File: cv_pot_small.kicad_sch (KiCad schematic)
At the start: 13 parts, among them J1 I/O connector, U1 HT7550-1, U2 TLV6001UIDBVR

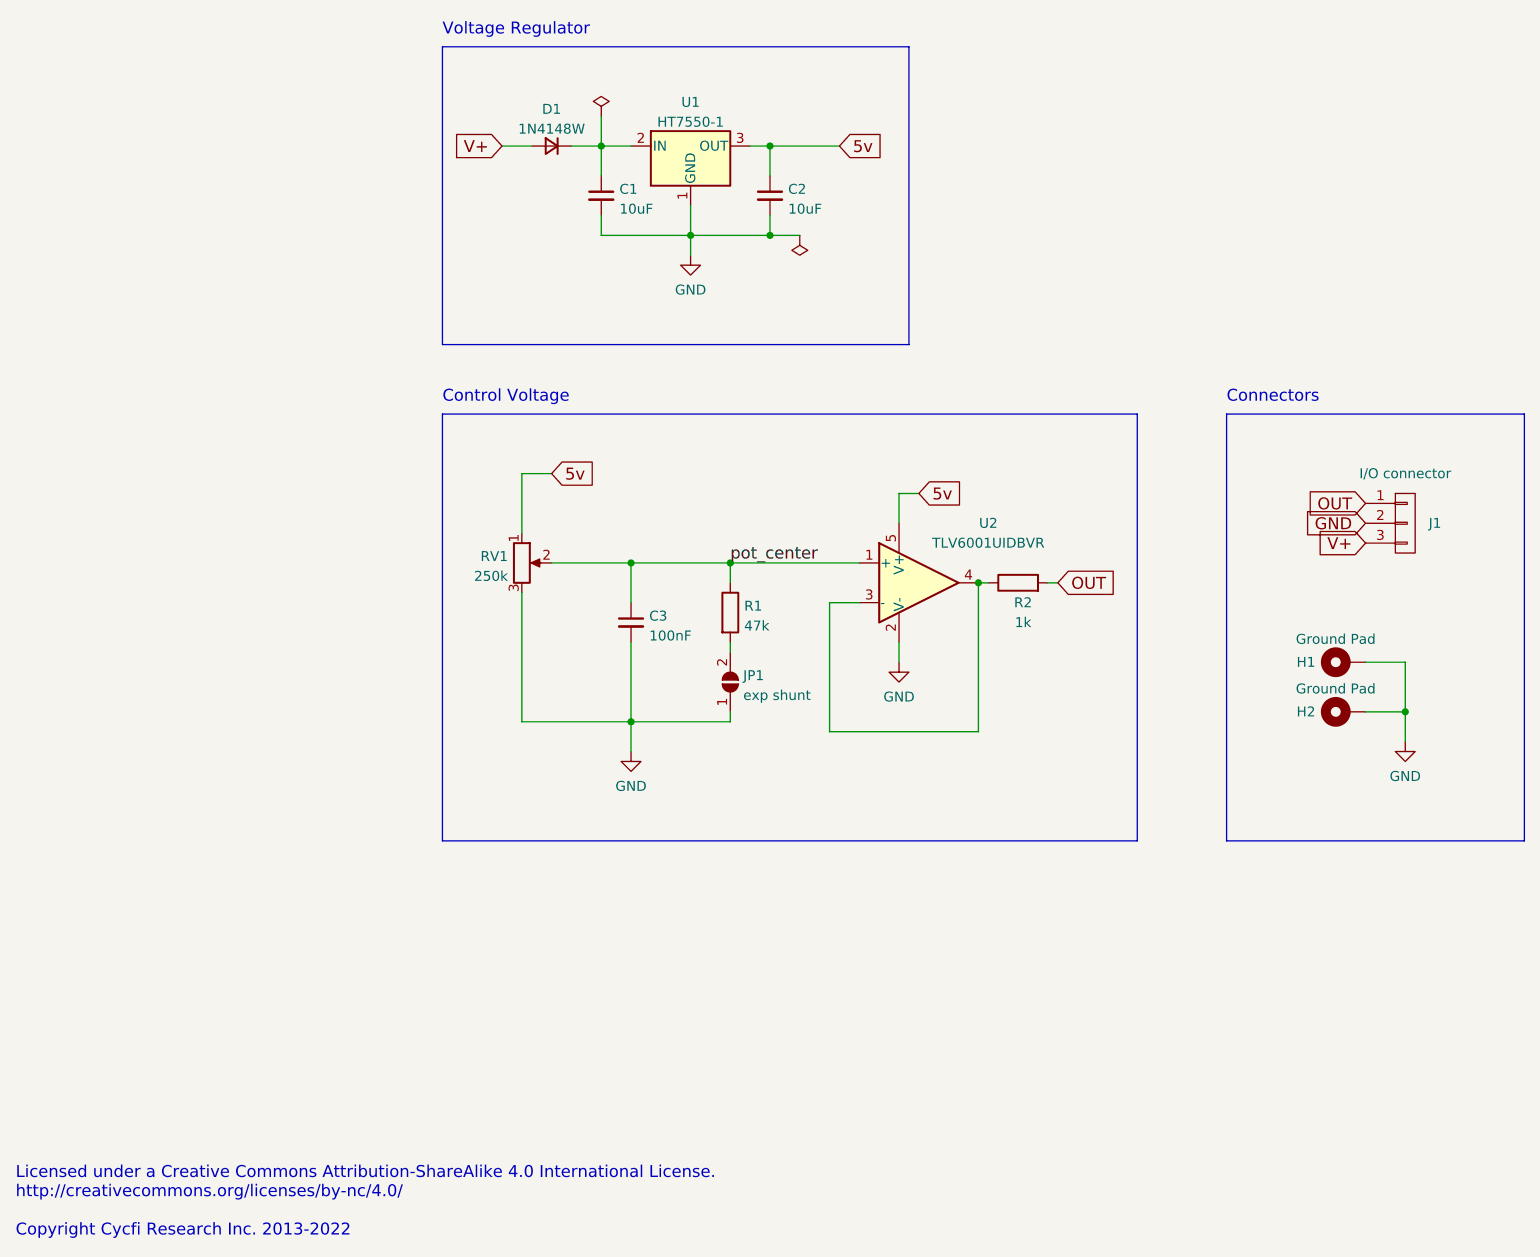
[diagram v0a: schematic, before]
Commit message: Convert the small CV pot to the 3.3V CV port standard
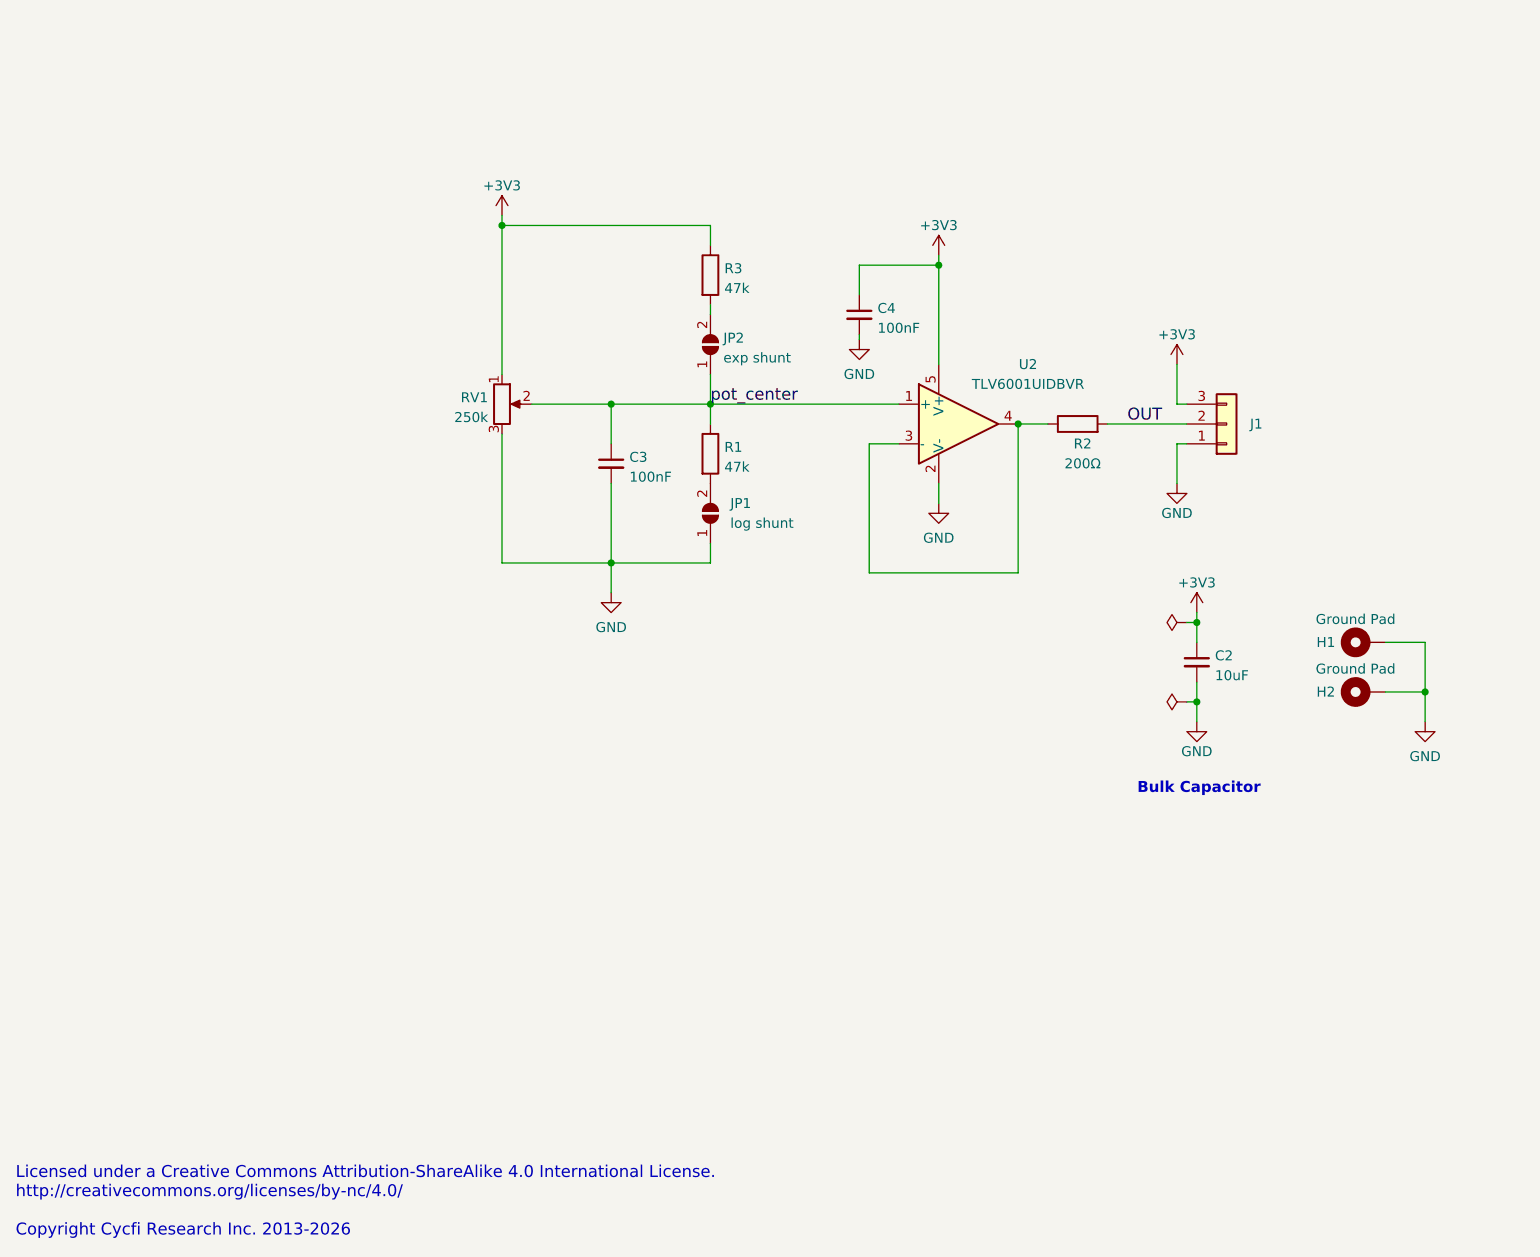
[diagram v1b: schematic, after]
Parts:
- removed C1: 10uF, Capacitor_SMD:C_0805_2012Metric, symbol Device:C_Small
- removed D1: 1N4148W, Diode_SMD:D_SOD-123, symbol Device:D_Small
- removed U1: HT7550-1, Package_TO_SOT_SMD:SOT-89-3, symbol cycfi_library:sot89-3-gio
- added C4: 100nF, Capacitor_SMD:C_0402_1005Metric, symbol Device:C_Small
- added JP2: exp shunt, Jumper:SolderJumper-2_P1.3mm_Open_TrianglePad1.0x1.5mm, symbol Jumper:SolderJumper_2_Open
- added R3: 47k, Resistor_SMD:R_0402_1005Metric, symbol Device:R
- J1: footprint cycfi_library:pin_header_1x3p_2.54mm_smd_horizontal -> Connector_JST:JST_SH_SM03B-SRSS-TB_1x03-1MP_P1.00mm_Horizontal; symbol cycfi_library:conn_1x3 -> Connector_Generic:Conn_01x03; LCSC (none) -> C160403
- JP1: value exp shunt -> log shunt
- R2: value 1k -> 200Ω; LCSC C11702 -> C25087
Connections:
- net V+ is gone; now on net +3V3: J1.3 (Pin_3)
- net GND: now also J1.1 (Pin_1), C4.2; no longer J1.2 (P2)
- net OUT: now also J1.2 (Pin_2); no longer J1.1 (P1)
- net pot_center: now also JP2.1 (A)
- net 5v renamed +3V3
- net +3V3: now also C4.1, R3.1
- new net: JP2.2 (B), R3.2
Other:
- note added: "Bulk Capacitor"
- note added: "Licensed under a Creative Commons Attribution-ShareAlike 4.0 International License. http://creativecommons.org/licenses/by-nc/4.0/ Copyright Cycfi Research Inc. 2013-2026"
- note removed: "Connectors"
- note removed: "Control Voltage"
- note removed: "Licensed under a Creative Commons Attribution-ShareAlike 4.0 International License. http://creativecommons.org/licenses/by-nc/4.0/ Copyright Cycfi Research Inc. 2013-2022"
- note removed: "Voltage Regulator"
- moved on the sheet: C2, C3, H1, H2, JP1, R1, R2, RV1, U2
